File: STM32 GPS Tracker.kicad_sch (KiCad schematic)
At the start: 46 parts, among them J3 693010020611, Q1 AO3407A, SW1 SW_Push, SW2 SW_Push, U1 SIM808, U2 TPS5430DDA, U3 SMF05CT1G, U4 STM32F030C8Tx, Y1 8MHz

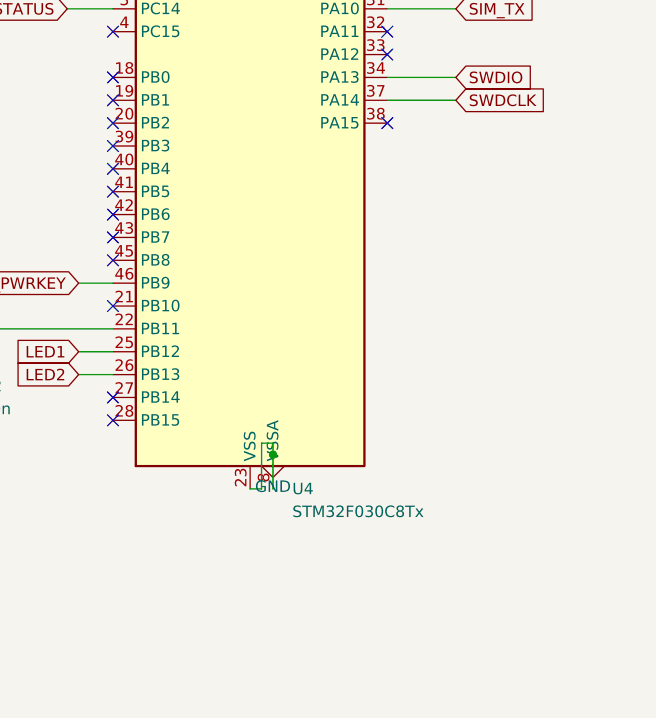
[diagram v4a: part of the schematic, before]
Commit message: Completed Placing and wiring components for STM32 ckt in Schematic
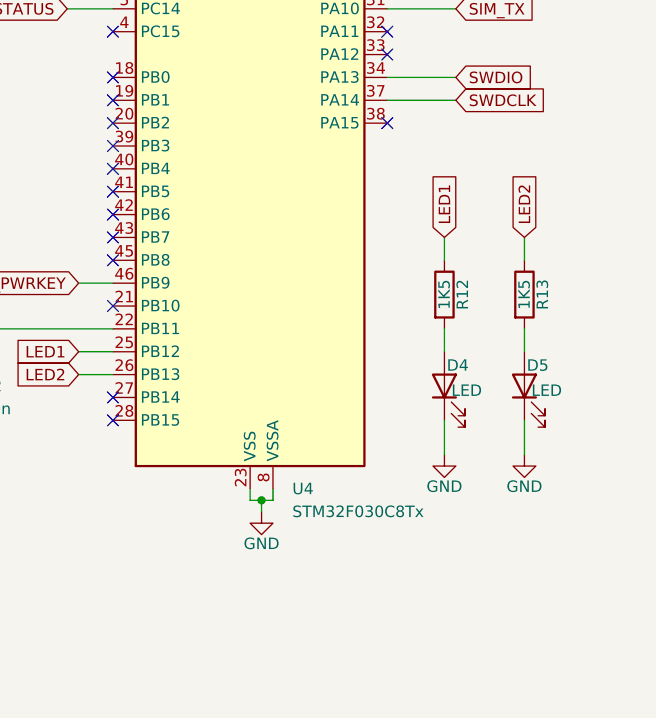
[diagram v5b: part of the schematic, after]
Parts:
- added D4, D5: LED, symbol Device:LED
- added R12, R13: 1K5, symbol Device:R
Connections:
- net GND: now also D4.1 (K), D5.1 (K)
- net LED1: now also R12.1
- net LED2: now also R13.1
- new net: D4.2 (A), R12.2
- new net: D5.2 (A), R13.2

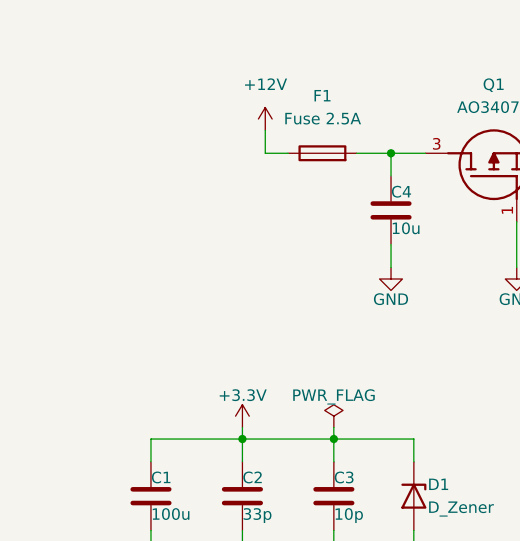
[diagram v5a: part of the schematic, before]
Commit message: Completed Placing and wiring components for Power Input ckt in Schematic
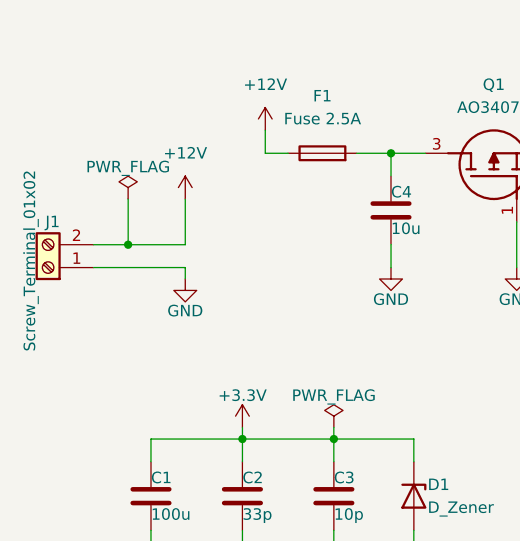
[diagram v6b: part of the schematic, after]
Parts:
- added J1: Screw_Terminal_01x02, symbol Connector:Screw_Terminal_01x02
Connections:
- net +12V: now also J1.2 (Pin_2)
- net GND: now also J1.1 (Pin_1)

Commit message: Completed Placing and wiring components for Connectors ckt in Schematic
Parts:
- added H1, H2, H3, H4: MountingHole_Pad, symbol Mechanical:MountingHole_Pad
- added J2, J4: Conn_01x08_Pin, symbol Connector:Conn_01x08_Pin
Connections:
- net +3.3V: now also J4.8 (Pin_8)
- net GND: now also J2.1 (Pin_1), J4.1 (Pin_1)
- net NRST: now also J2.3 (Pin_3)
- net PA4: now also J4.5 (Pin_5)
- net PA5/SPI1_CLK: now also J4.4 (Pin_4)
- net PA6/SPI1_MISO: now also J4.3 (Pin_3)
- net PA7/SPI1_MOSI: now also J4.2 (Pin_2)
- net SIM_PWRKEY: now also J2.8 (Pin_8)
- net SIM_RESET: now also J2.5 (Pin_5)
- net SIM_RX: now also J2.6 (Pin_6)
- net SIM_TX: now also J2.7 (Pin_7)
- net SWDCLK: now also J2.4 (Pin_4)
- net SWDIO: now also J2.2 (Pin_2)
- net USART2_RX: now also J4.6 (Pin_6)
- net USART2_TX: now also J4.7 (Pin_7)

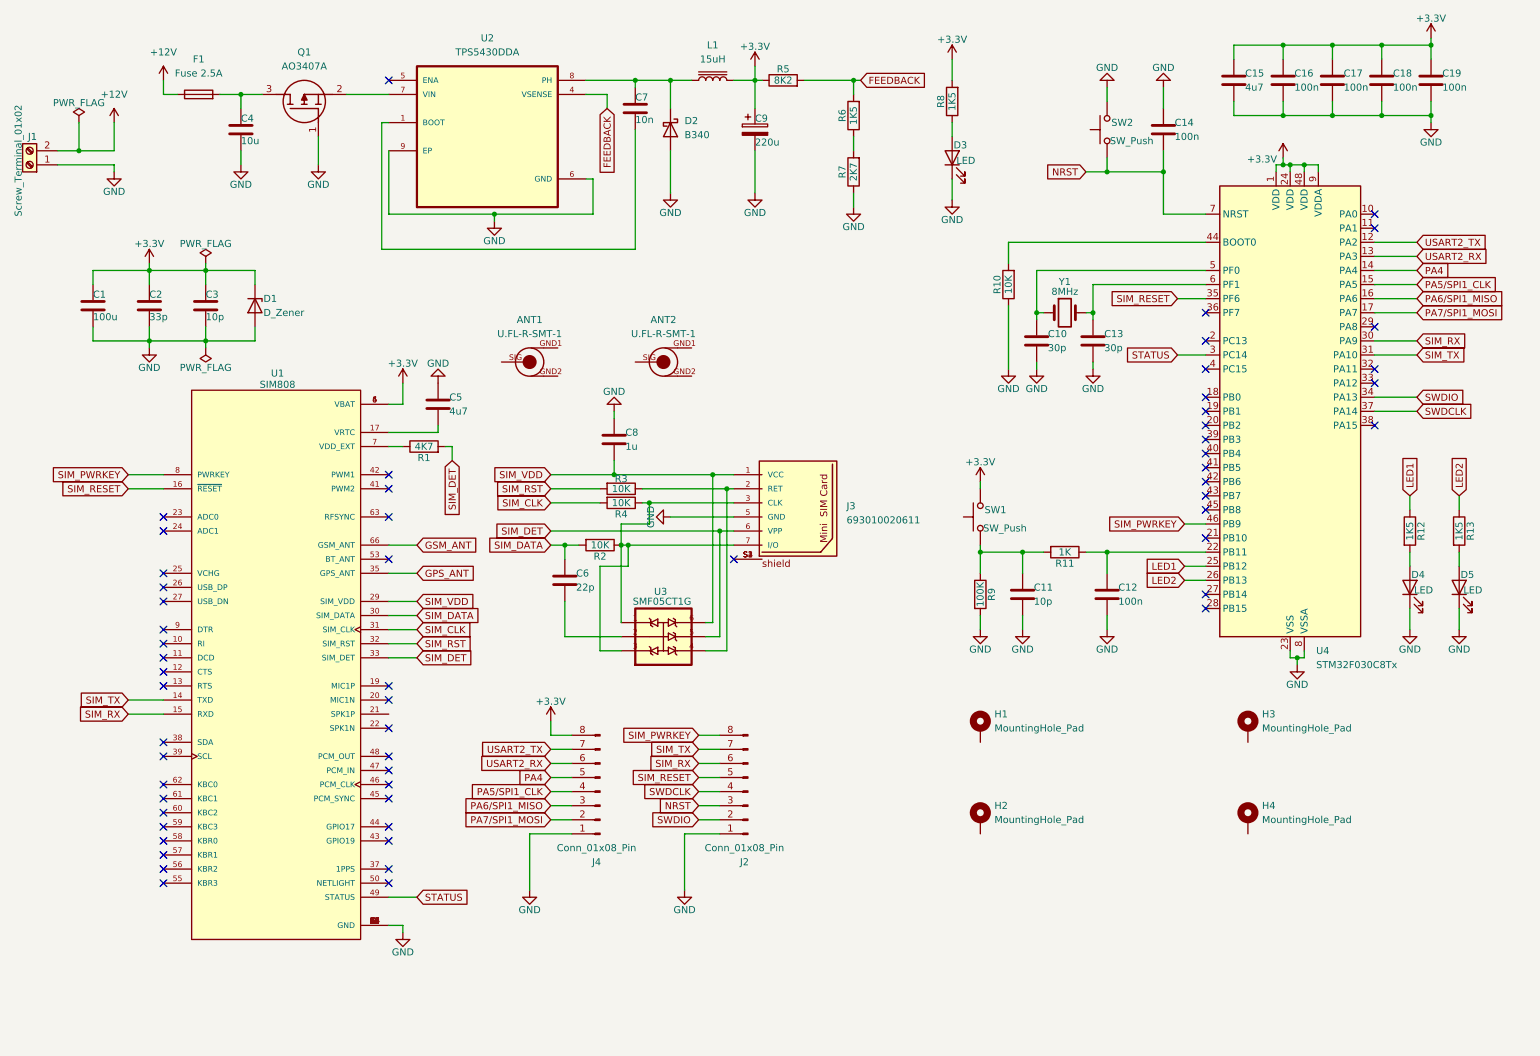
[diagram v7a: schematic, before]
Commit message: Placed the Lines in Schematic
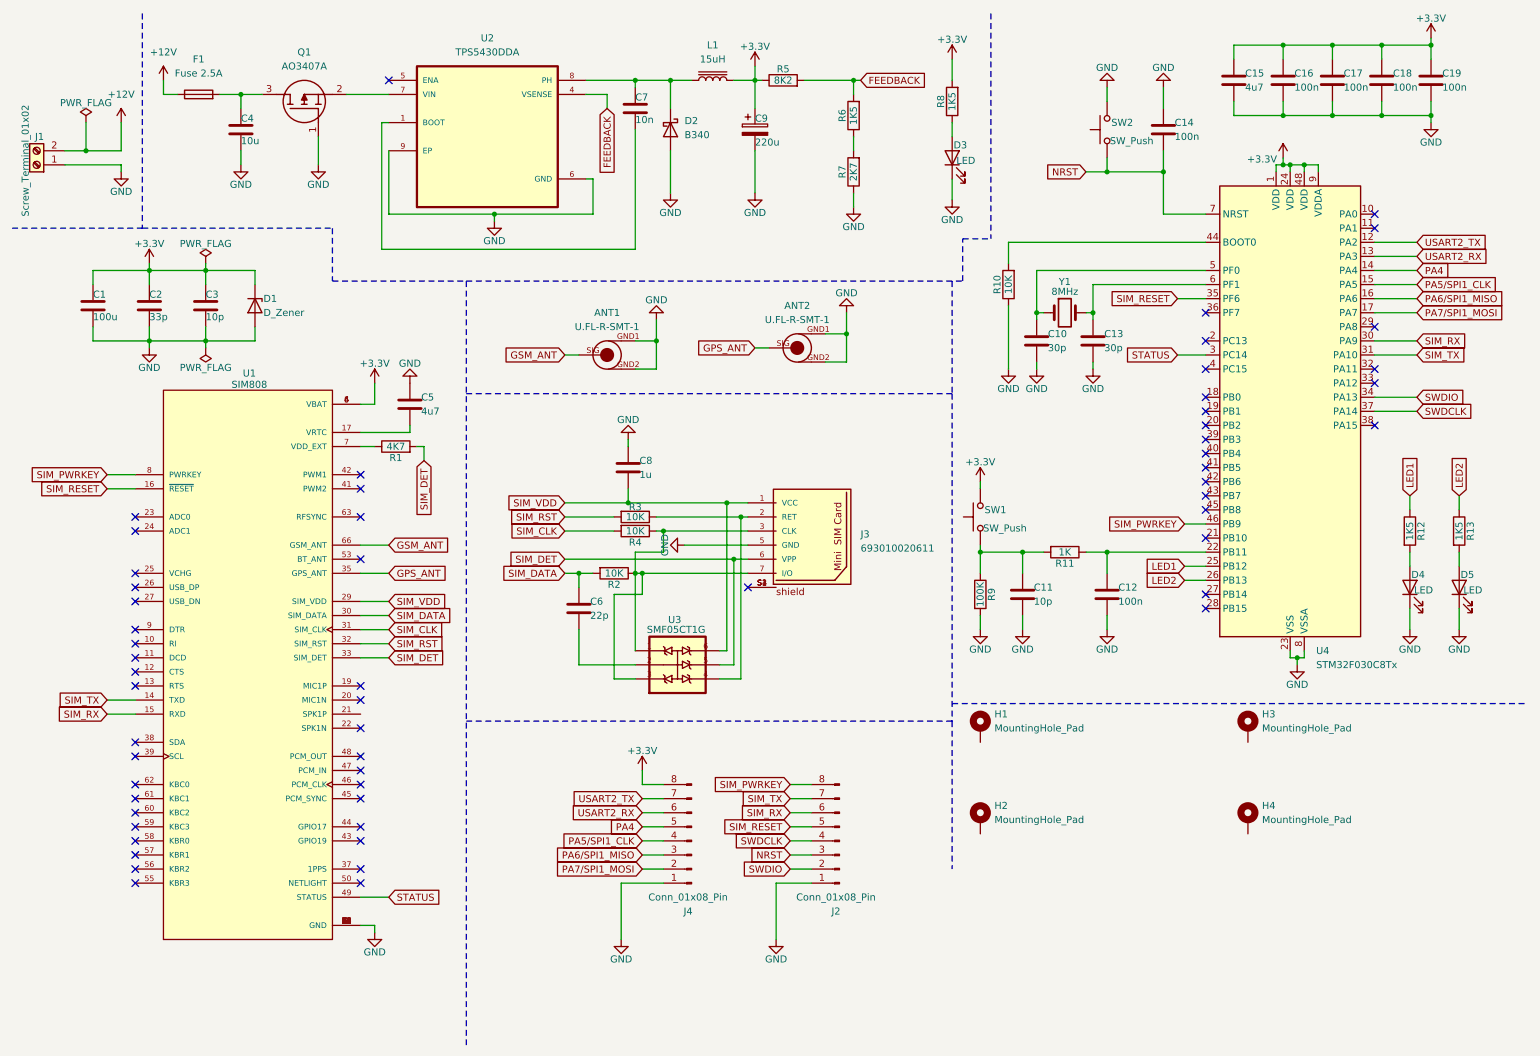
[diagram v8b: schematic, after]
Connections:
- net GND: now also ANT1.GND1, ANT1.GND2, ANT2.GND1, ANT2.GND2
- net GPS_ANT: now also ANT2.SIG
- net GSM_ANT: now also ANT1.SIG
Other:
- moved on the sheet: ANT1, ANT2, C5, C6, C8, J1, J2, J3, J4, R1, R2, R3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
